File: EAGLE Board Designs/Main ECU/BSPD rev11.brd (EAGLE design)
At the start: 160 x 100 mm, 45 parts, among them Q1 P-CHANNEL_MOSFET_DMP3099L-7, U11 SN74AHC1G09, U17 OPA990IDBVR, U19 OPA990IDBVR, U28 OPA990IDBVR, U29 OPA990IDBVR, U6 OPA990IDBVR, X1 CONNECTOR-4NANO-FIT-VERTICAL-4, X2 CONNECTOR-4NANO-FIT-VERTICAL-4

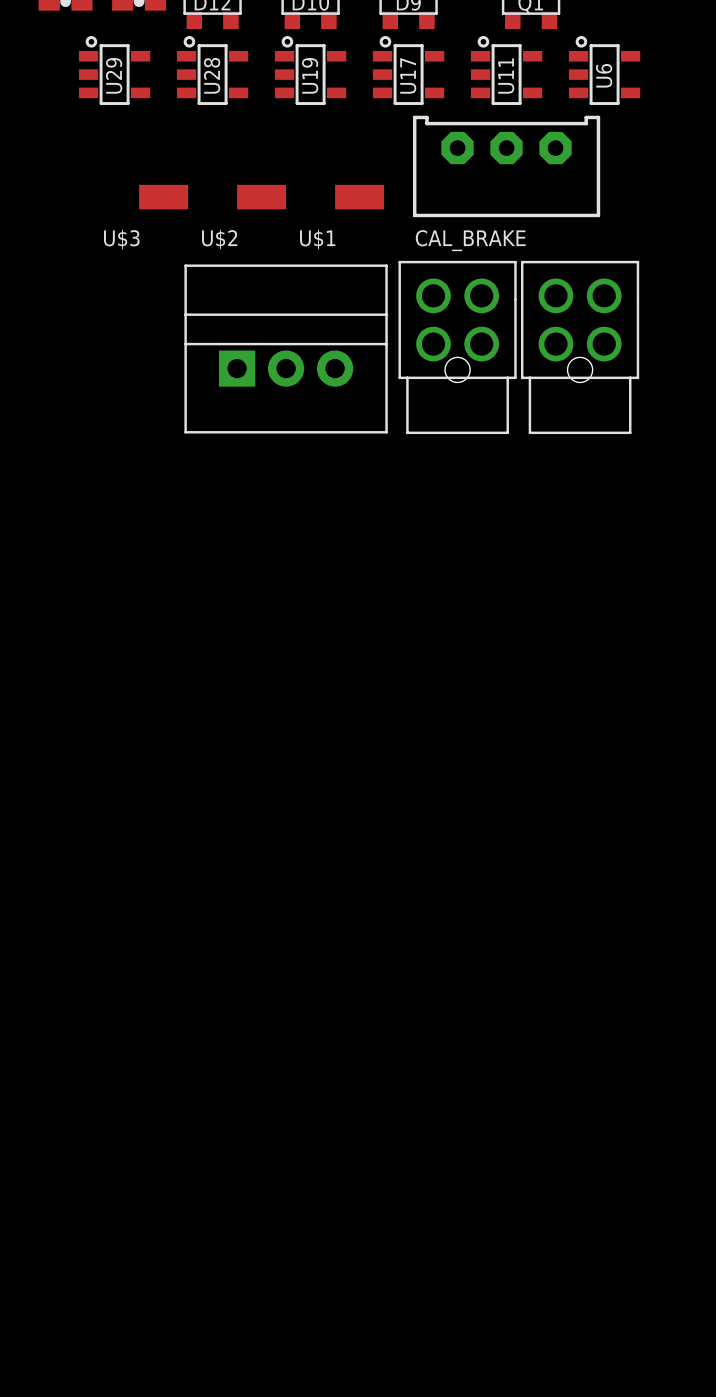
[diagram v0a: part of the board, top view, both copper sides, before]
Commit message: Improvements to make debugging easier
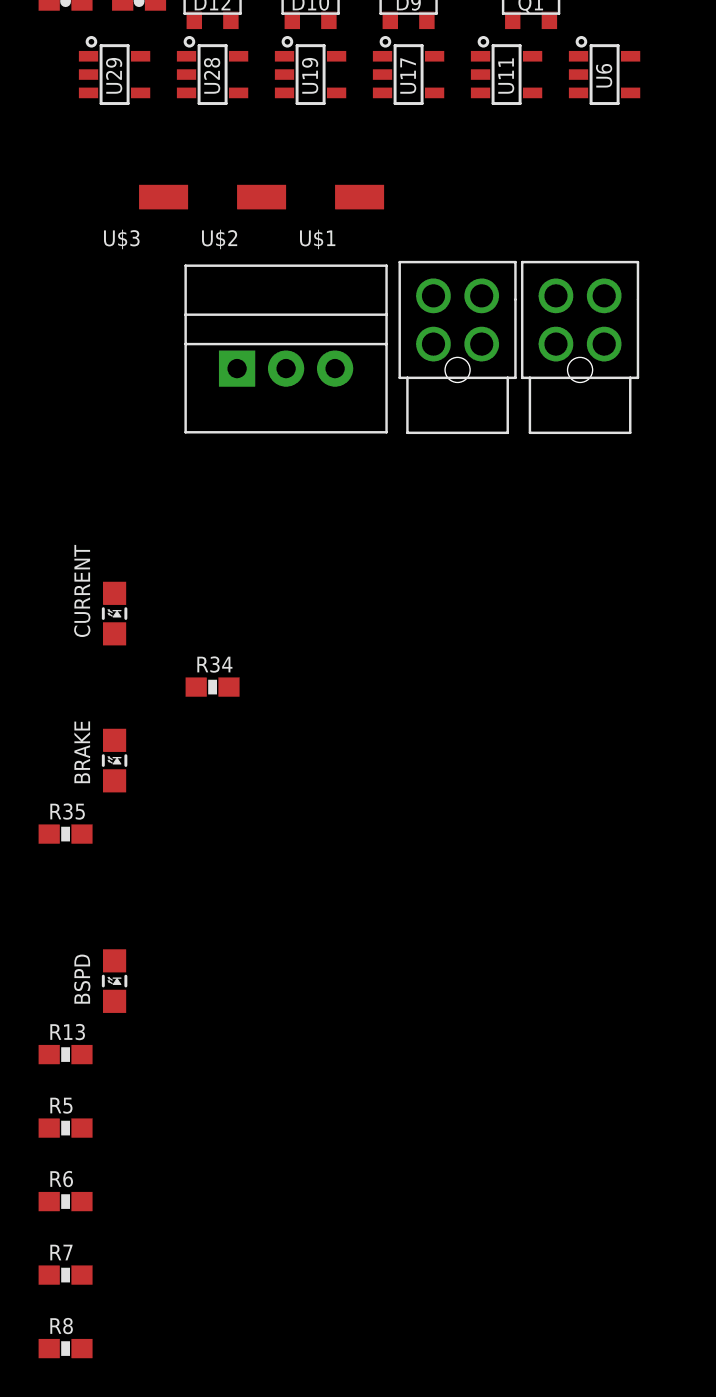
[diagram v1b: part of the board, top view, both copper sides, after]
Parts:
- removed CAL_BRAKE: (no value), HyTechDevices:TRIMPOT_3296
- added BRAKE: Red, HyTechDevices:LED-805
- added BSPD: Orange, HyTechDevices:LED-805
- added CURRENT: Yellow, HyTechDevices:LED-805
- added R13: 976, HyTechDevices:0603-RES
- added R34: 324, HyTechDevices:0603-RES
- added R35: 215, HyTechDevices:0603-RES
- added R5, R6: 10M, HyTechDevices:0603-RES
- added R7: 31600, HyTechDevices:0603-RES
- added R8: 5110, HyTechDevices:0603-RES
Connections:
- removed net N$109: C9.1, R32.1, R33.1, U6.3
- new net GND1: BRAKE.C, BSPD.C, CURRENT.C
- new net N$102: CURRENT.A, R35.2
- new net N$103: BRAKE.A, R34.2
- new net N$108: BSPD.A, R13.2
- new net V_CAP: C9.1, R32.1, R33.1, U6.3, X2.P$3
- net +5V: now also R7.2; no longer CAL_BRAKE.1
- net BRAKE_HIGH: now also R34.1
- net BRAKE_LOW_DIV: now also R6.2
- net BSPD_OK: now also R13.1, X2.P$4
- net CURRENT_HIGH: now also R35.1
- net CURRENT_LOW_DIV: now also R5.2
- net GND: now also R5.1, R6.1, R8.1; no longer CAL_BRAKE.3
- net N$15: now also R7.1, R8.2; no longer CAL_BRAKE.2

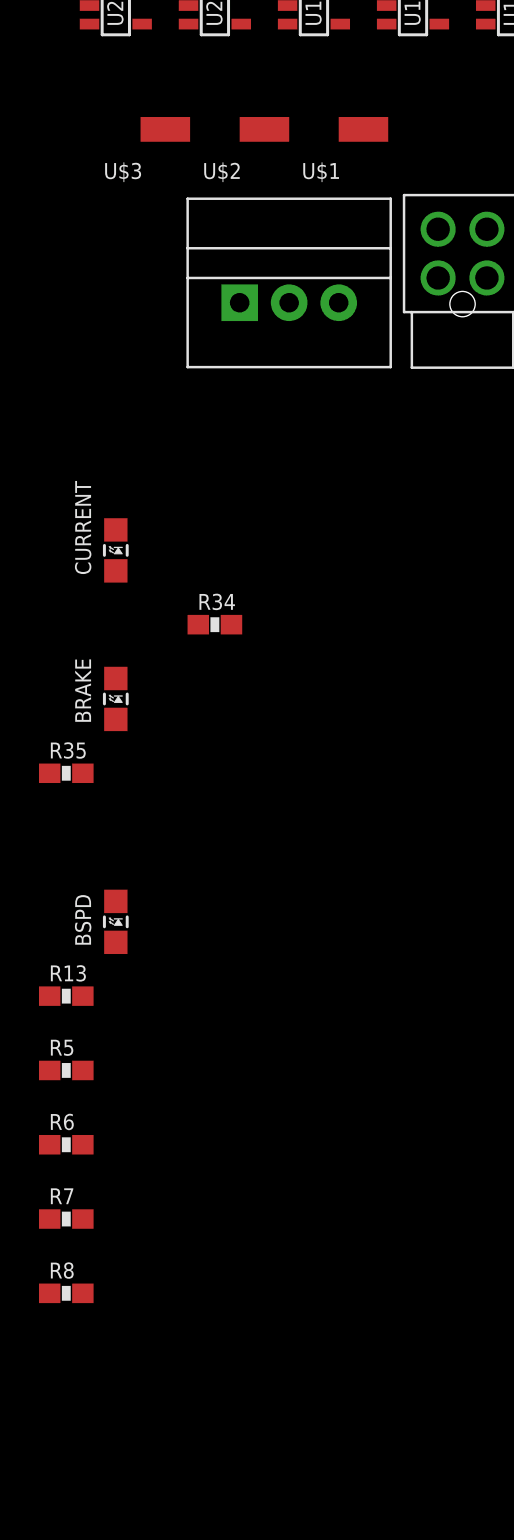
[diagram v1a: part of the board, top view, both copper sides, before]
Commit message: Changed what touch pads connect to
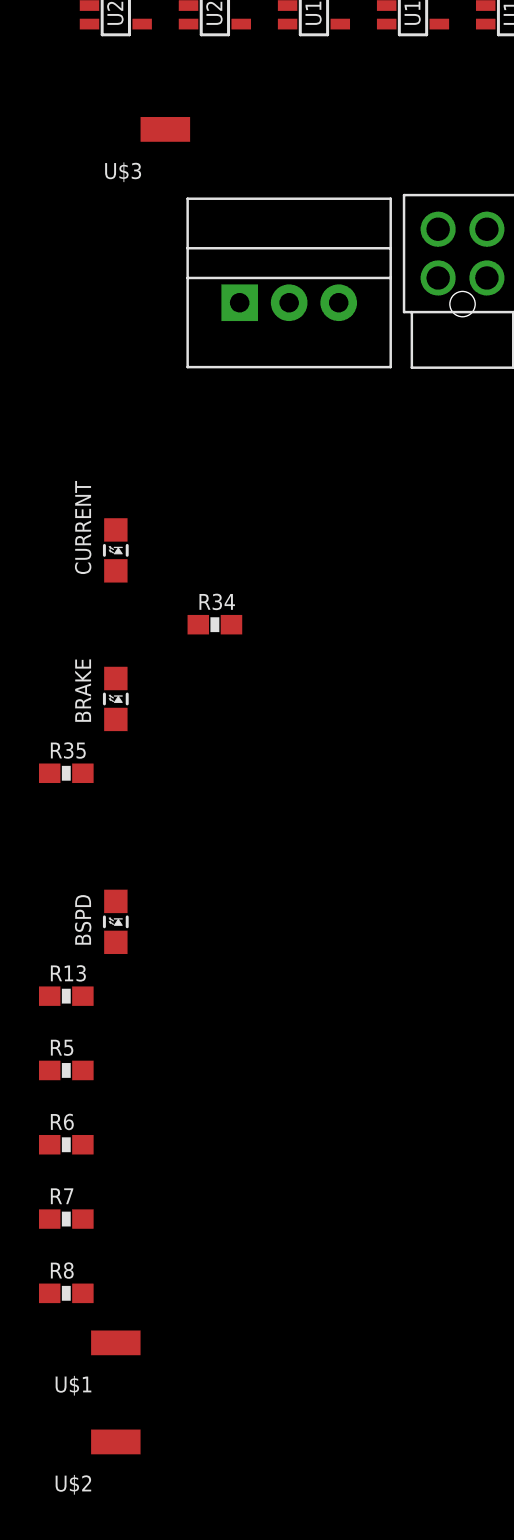
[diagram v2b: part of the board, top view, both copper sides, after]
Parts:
- moved U$2 67.7 mm to (-40.6, -54.6)
- moved U$1 63.5 mm to (-40.6, -49.5)
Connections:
- net BRAKE_HIGH: no longer U$2.P$1
- net BRAKE_LOW_DIV: now also U$1.P$1
- net CURRENT_HIGH: no longer U$1.P$1
- net CURRENT_LOW_DIV: now also U$2.P$1
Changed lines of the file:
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@@
 </element>
 <element name="REG2" library="HyTechDevices" package="OKI-78SR" value="5V" x="-31.75" y="3.81" smashed="yes"/>
-<element name="U$1" library="HyTechDevices" package="SOLDER_PAD_XSMALL" value="SOLDER_PAD" x="-27.94" y="12.7" smashed="yes">
-<attribute name="NAME" x="-31.115" y="10.16" size="0.8128" layer="25" font="vector"/>
-</element>
-<element name="U$2" library="HyTechDevices" package="SOLDER_PAD_XSMALL" value="SOLDER_PAD" x="-33.02" y="12.7" smashed="yes">
-<attribute name="NAME" x="-36.195" y="10.16" size="0.8128" layer="25" font="vector"/>
-</element>
 <element name="U$3" library="HyTechDevices" package="SOLDER_PAD_XSMALL" value="SOLDER_PAD" x="-38.1" y="12.7" smashed="yes">
 <attribute name="NAME" x="-41.275" y="10.16" size="0.8128" layer="25" font="vector"/>
@@
 <element name="R8" library="HyTechDevices" package="0603-RES" value="5110" x="-43.18" y="-46.99" smashed="yes">
 <attribute name="NAME" x="-44.069" y="-46.228" size="0.8128" layer="25" font="vector"/>
+</element>
+<element name="U$1" library="HyTechDevices" package="SOLDER_PAD_XSMALL" value="SOLDER_PAD" x="-40.64" y="-49.53" smashed="yes">
+<attribute name="NAME" x="-43.815" y="-52.07" size="0.8128" layer="25"/>
+</element>
+<element name="U$2" library="HyTechDevices" package="SOLDER_PAD_XSMALL" value="SOLDER_PAD" x="-40.64" y="-54.61" smashed="yes">
+<attribute name="NAME" x="-43.815" y="-57.15" size="0.8128" layer="25"/>
 </element>
 </elements>
@@
 <contactref element="U11" pad="1"/>
 <contactref element="U19" pad="1"/>
-<contactref element="U$1" pad="P$1"/>
 <contactref element="R35" pad="1"/>
-<wire x1="-27.94" y1="12.7" x2="-44.03" y2="-20.32" width="0" layer="19" extent="1-1"/>
-<wire x1="-31.83" y1="20" x2="-27.94" y2="12.7" width="0" layer="19" extent="1-1"/>
-<wire x1="-21.67" y1="20" x2="-27.94" y2="12.7" width="0" layer="19" extent="1-1"/>
+<wire x1="-31.83" y1="20" x2="-44.03" y2="-20.32" width="0" layer="19" extent="1-1"/>
+<wire x1="-21.67" y1="20" x2="-31.83" y2="20" width="0" layer="19" extent="1-1"/>
 </signal>
 <signal name="BRAKE_HIGH">
 <contactref element="U11" pad="2"/>
 <contactref element="U28" pad="1"/>
-<contactref element="U$2" pad="P$1"/>
 <contactref element="R34" pad="1"/>
-<wire x1="-33.02" y1="12.7" x2="-36.41" y2="-12.7" width="0" layer="19" extent="1-1"/>
-<wire x1="-36.91" y1="20" x2="-33.02" y2="12.7" width="0" layer="19" extent="1-1"/>
-<wire x1="-21.67" y1="19.05" x2="-33.02" y2="12.7" width="0" layer="19" extent="1-1"/>
+<wire x1="-36.91" y1="20" x2="-36.41" y2="-12.7" width="0" layer="19" extent="1-1"/>
+<wire x1="-21.67" y1="19.05" x2="-36.91" y2="20" width="0" layer="19" extent="1-1"/>
 </signal>
 <signal name="CURRENT_LOW_DIV">
@@
 <contactref element="U19" pad="3"/>
 <contactref element="R5" pad="2"/>
+<contactref element="U$2" pad="P$1"/>
+<wire x1="-42.33" y1="-35.56" x2="-40.64" y2="-54.61" width="0" layer="19" extent="1-1"/>
 <wire x1="-31.83" y1="18.1" x2="-42.33" y2="-35.56" width="0" layer="19" extent="1-1"/>
 <wire x1="-38.95" y1="34.29" x2="-31.83" y2="18.1" width="0" layer="19" extent="1-1"/>
@@
 <contactref element="U28" pad="3"/>
 <contactref element="R6" pad="2"/>
+<contactref element="U$1" pad="P$1"/>
+<wire x1="-42.33" y1="-39.37" x2="-40.64" y2="-49.53" width="0" layer="19" extent="1-1"/>
 <wire x1="-36.91" y1="18.1" x2="-42.33" y2="-39.37" width="0" layer="19" extent="1-1"/>
 <wire x1="-19.9" y1="30.48" x2="-36.91" y2="18.1" width="0" layer="19" extent="1-1"/>

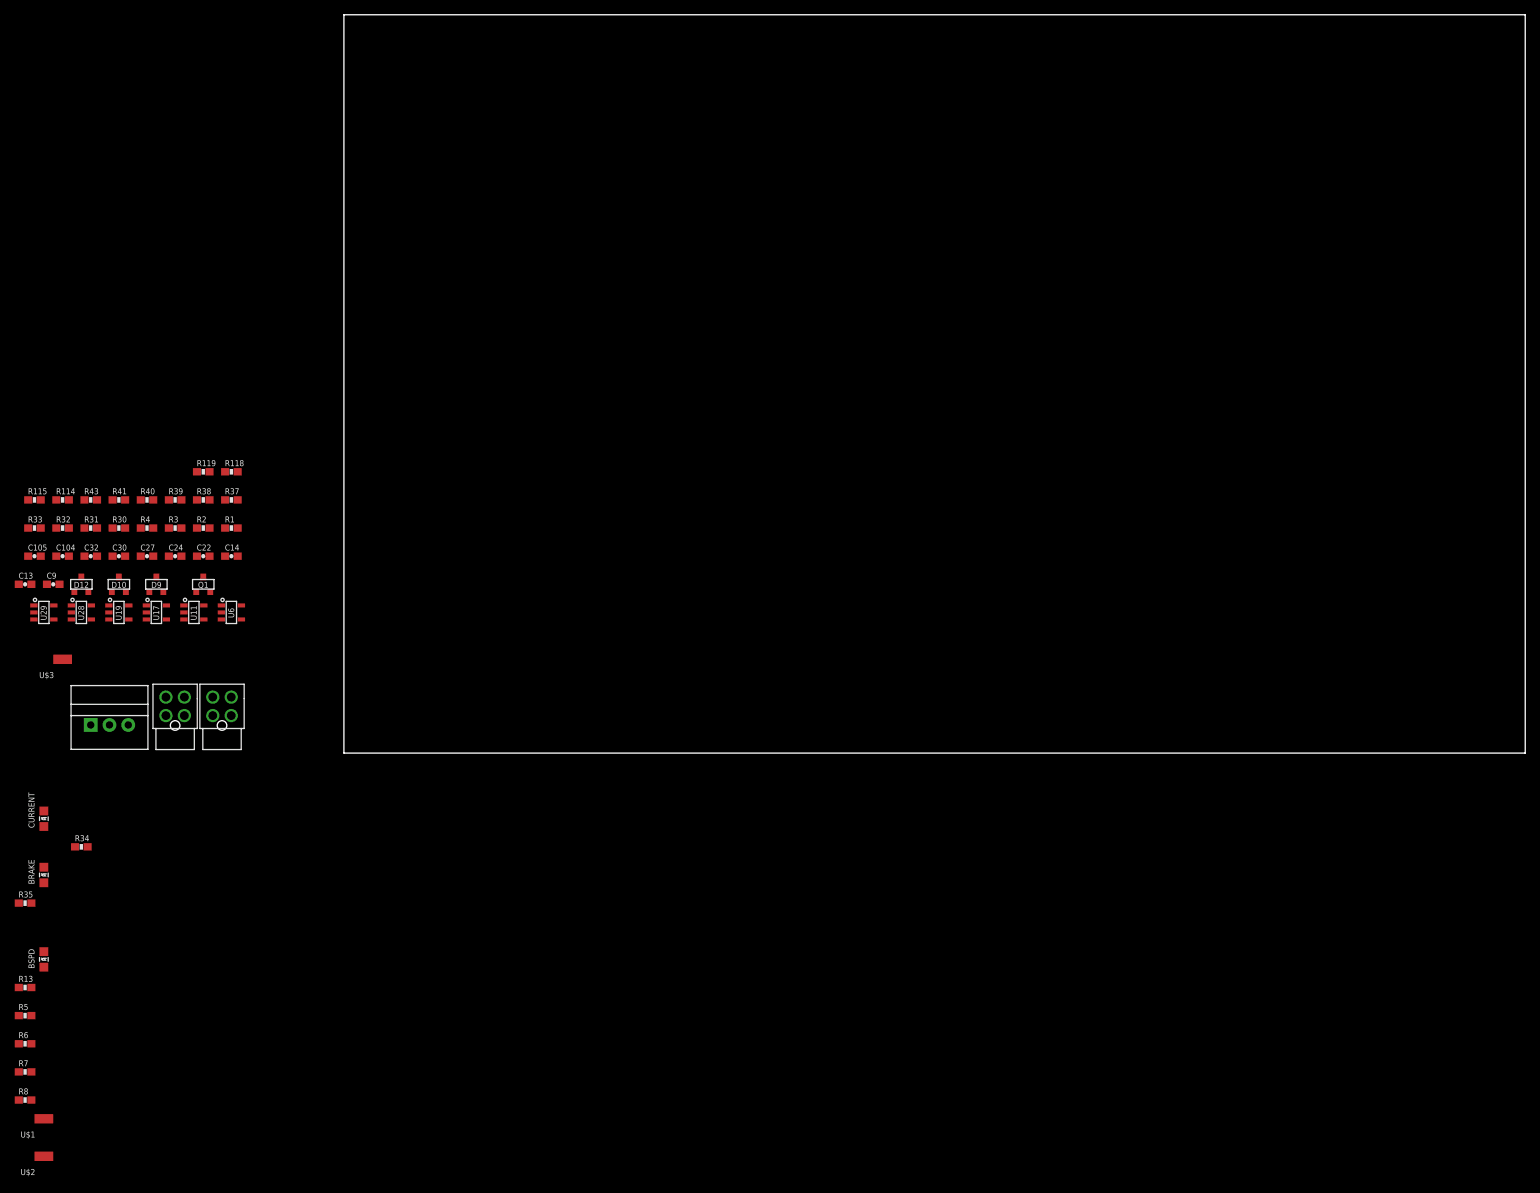
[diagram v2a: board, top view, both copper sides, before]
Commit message: Laid out BSPDrev11 schematic on board
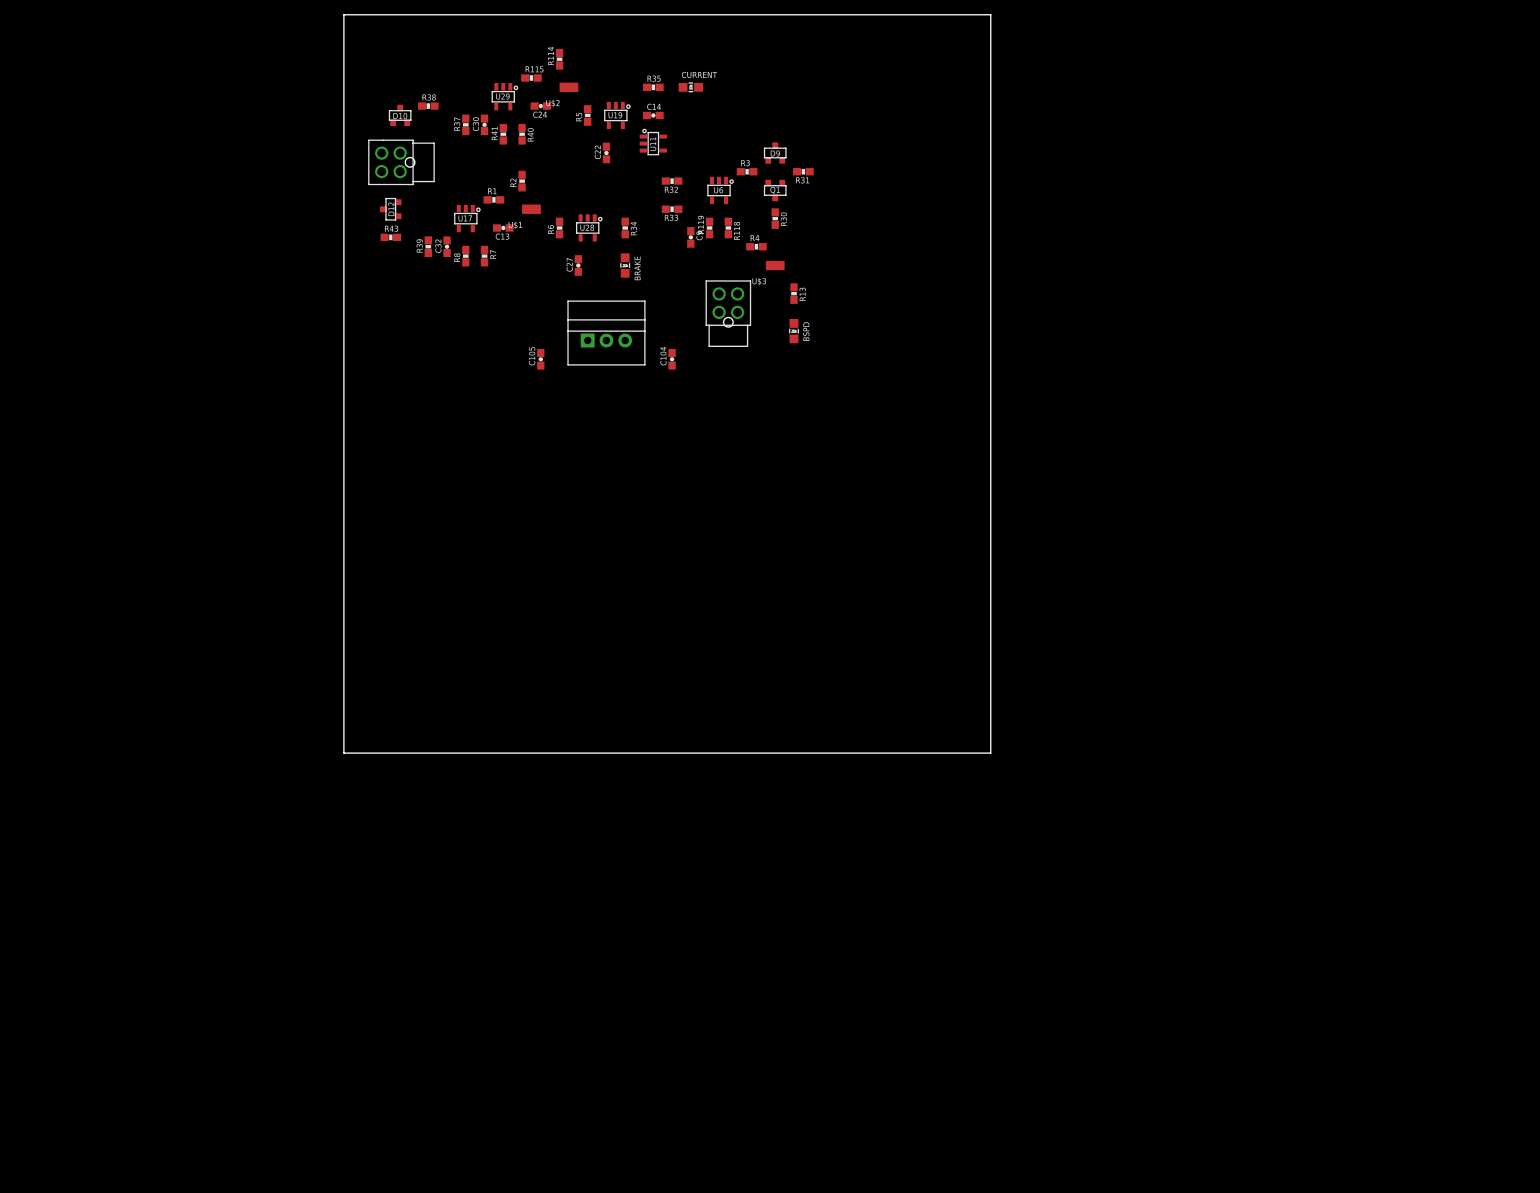
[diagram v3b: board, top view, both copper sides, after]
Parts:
- moved U$2 161.3 mm to (30.5, 90.2)
- moved R5 143.8 mm to (33.0, 86.4), turned to 90 degrees
- moved R13 140.3 mm to (61.0, 62.2), turned to 270 degrees
- moved U$1 139.8 mm to (25.4, 73.7)
- moved R35 139.5 mm to (41.9, 90.2)
- moved BSPD 132.5 mm to (61.0, 57.1), turned to 180 degrees
- moved CURRENT 132.3 mm to (47.0, 90.2), turned to 270 degrees
- moved R6 132.1 mm to (29.2, 71.1), turned to 90 degrees
- moved R8 128.9 mm to (16.5, 67.3), turned to 90 degrees
- moved R7 126.8 mm to (19.1, 67.3), turned to 270 degrees
- moved BRAKE 114.1 mm to (38.1, 66.0), turned to 180 degrees
- moved R34 111.6 mm to (38.1, 71.1), turned to 270 degrees
- moved U$3 110.3 mm to (58.4, 66.0)
- moved R31 107.9 mm to (62.2, 78.7), turned to 180 degrees
- moved D9 102.2 mm to (58.4, 81.3)
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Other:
- board size 160 x 100 mm -> 87.6 x 100 mm
